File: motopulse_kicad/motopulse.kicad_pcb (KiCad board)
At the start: 2 copper layers, 100 x 95 mm, 12 parts, among them J1 ESP32-S3_Left_Header, J2 ESP32-S3_Right_Header, J3 INMP441_Breakout, J4 OLED_0.96_I2C

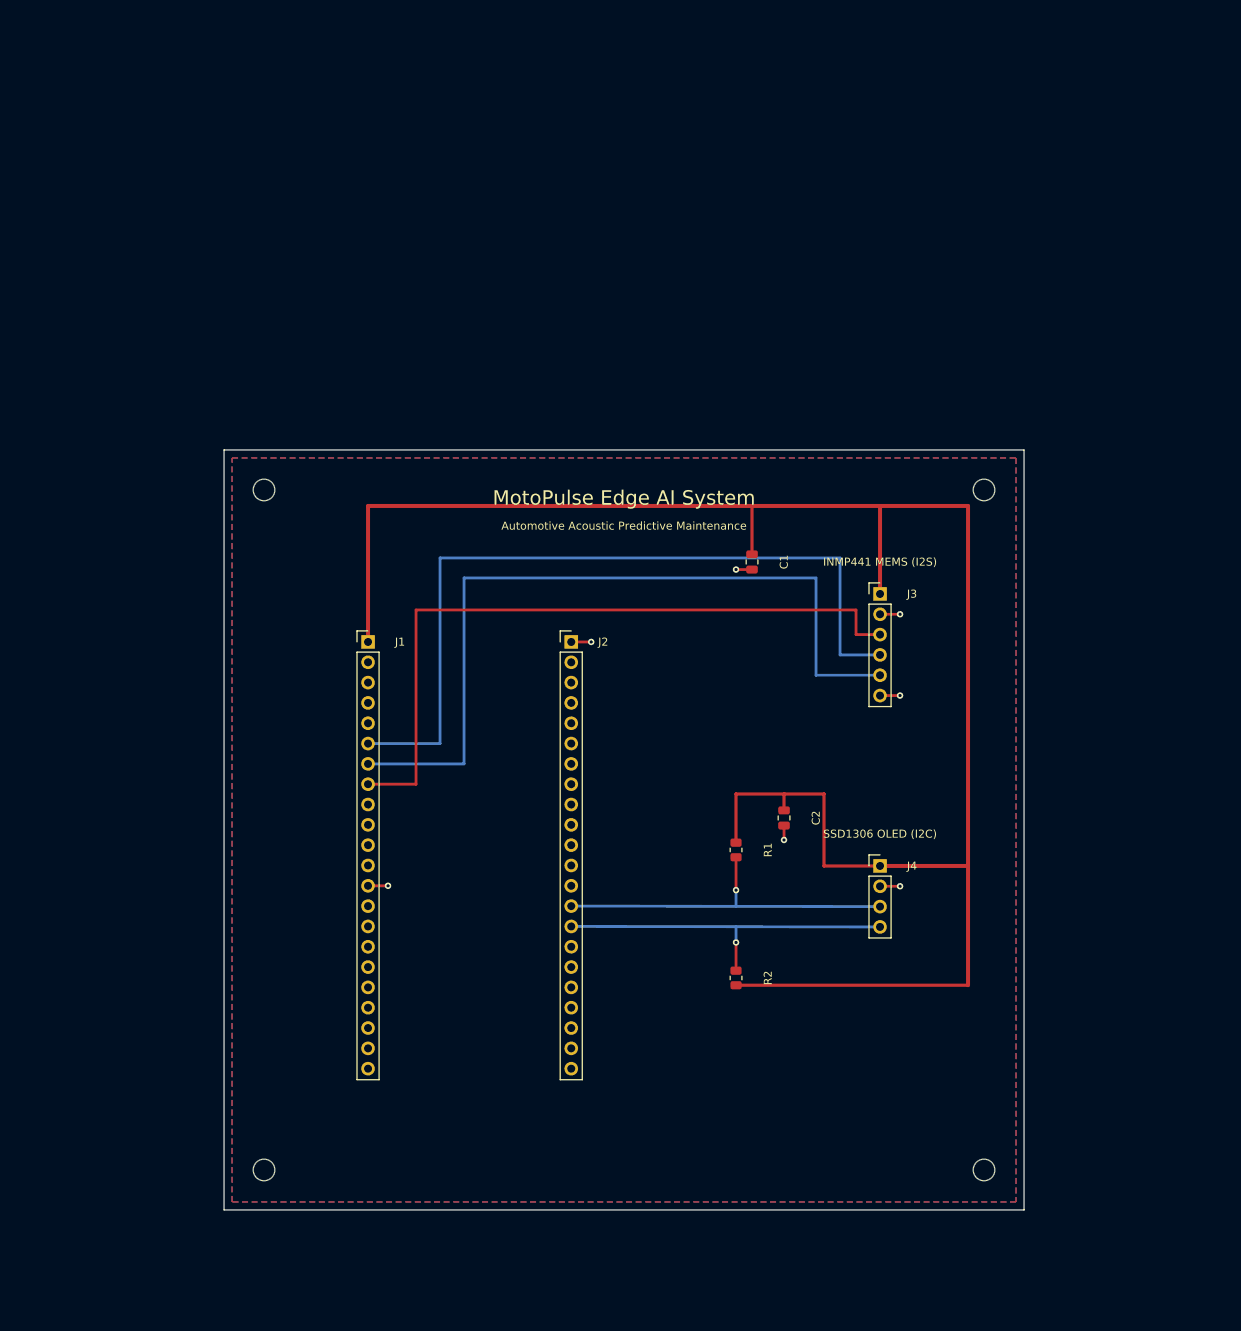
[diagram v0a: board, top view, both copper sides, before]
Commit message: feat(hardware): unified ESP32-S3 carrier with 40mm dual mic, OLED, piezo and zero-capacitor layout
- ESP32-S3-DevKitC-1 (2x22 headers) unified motherboard
- Dual INMP441 MEMS microphones with exactly 40.0 mm baseline spacing
- 0.96 inch SSD1306 OLED display header
- Piezoelectric vibration sensor connector and 1M damping resistor
- Zero capacitors, pure direct-connect architecture
- KiCad ERC 0 errors, PCB DRC 0 violations, 0 unconnected items

Co-authored-by: ishannvn <ishannvn@users.noreply.github.com>
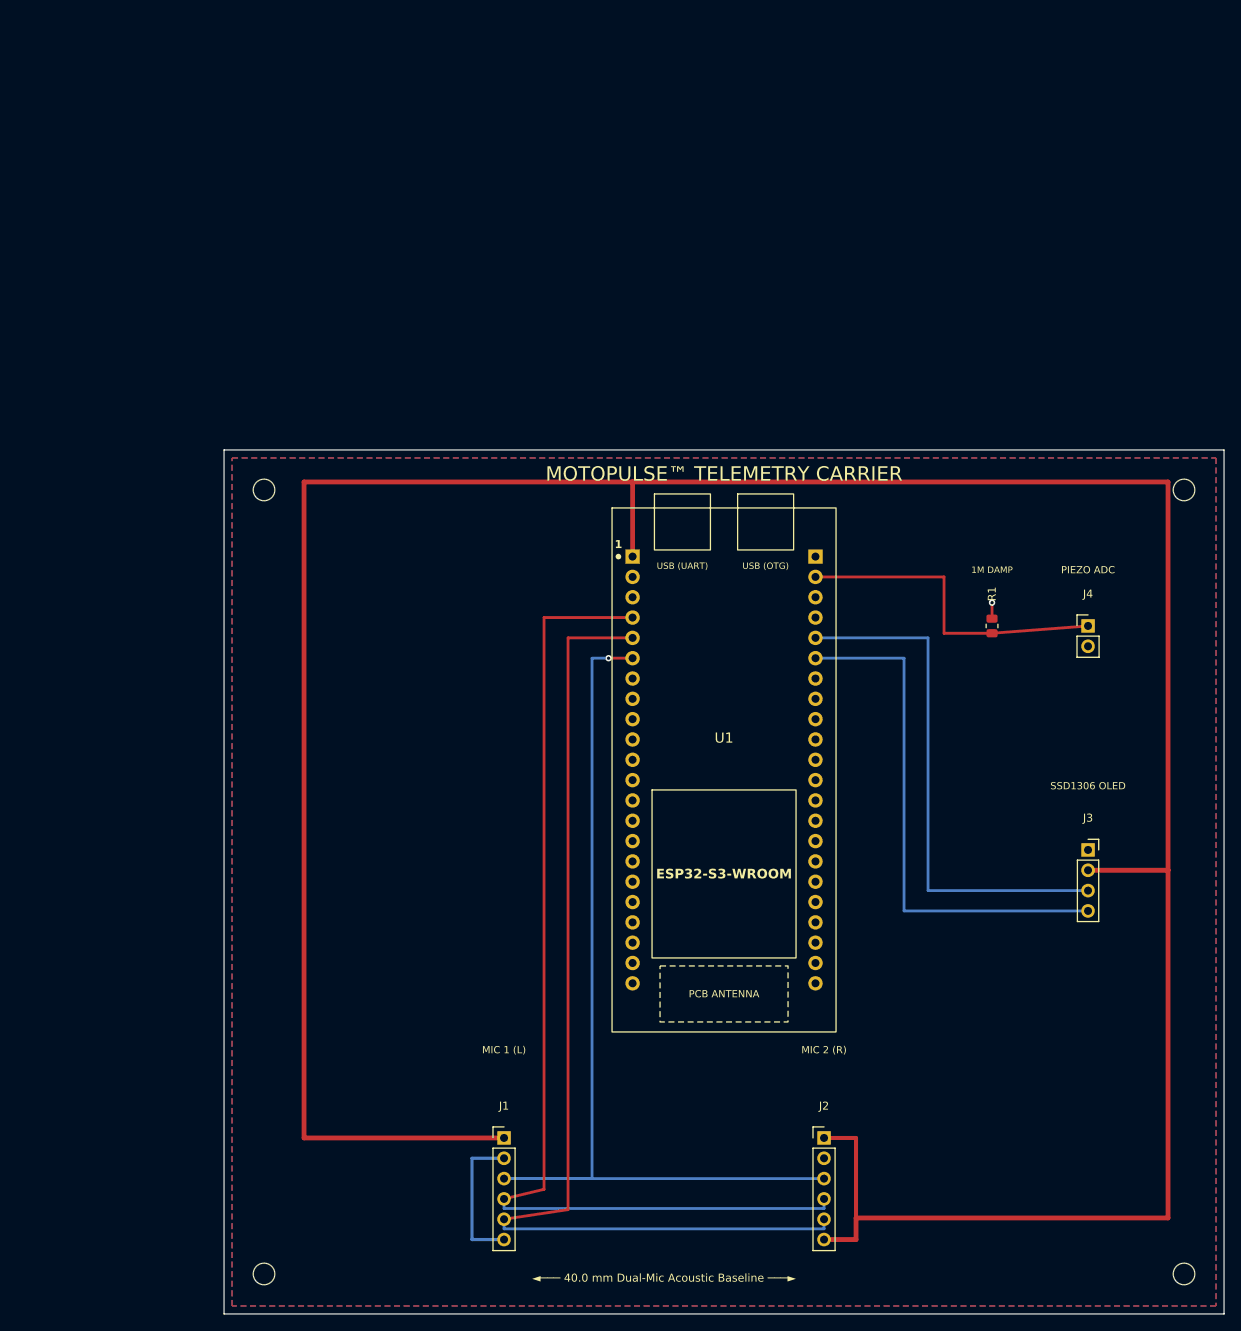
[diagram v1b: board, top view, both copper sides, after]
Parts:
- removed C1, C2: 100nF, C_0805_2012Metric
- removed R2: 4.7k, R_0805_2012Metric
- added U1: ESP32-S3-DevKitC-1, ESP32-S3-DevKitC-1, F.Cu at (162.5, 140.0)
- J1: value ESP32-S3_Left_Header -> INMP441_Left; footprint PinHeader_1x22_P2.54mm_Vertical -> PinHeader_1x06_P2.54mm_Vertical
- J2: value ESP32-S3_Right_Header -> INMP441_Right; footprint PinHeader_1x22_P2.54mm_Vertical -> PinHeader_1x06_P2.54mm_Vertical
- J3: value INMP441_Breakout -> SSD1306_OLED; footprint PinHeader_1x06_P2.54mm_Vertical -> PinSocket_1x04_P2.54mm_Vertical
- J4: value OLED_0.96_I2C -> Piezo_Sensor; footprint PinHeader_1x04_P2.54mm_Vertical -> PinHeader_1x02_P2.54mm_Vertical
- R1: value 4.7k -> 1.0M
- moved J2 69.6 mm to (175.0, 186.0)
- moved J1 64.3 mm to (135.0, 186.0)
- moved R1 42.5 mm to (196.0, 122.0), turned to 90 degrees
- moved J3 41.2 mm to (208.0, 150.0)
- moved J4 39.7 mm to (208.0, 122.0)
- moved H4 28.2 mm to (220.0, 203.0)
- moved H2 25.0 mm to (220.0, 105.0)
- moved H3 13.0 mm to (105.0, 203.0)
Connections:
- J1 pad 2: unconnected-(J1-Pin_2-Pad2) -> GND
- J1 pad 3: unconnected-(J1-Pin_3-Pad3) -> /I2S_SD
- J1 pad 4: unconnected-(J1-Pin_4-Pad4) -> /I2S_SCK
- J1 pad 5: unconnected-(J1-Pin_5-Pad5) -> /I2S_WS
- J1 pad 6: /I2S_SCK -> GND
- J2 pad 1: GND -> +3.3V
- J2 pad 2: unconnected-(J2-Pin_2-Pad2) -> GND
- J2 pad 3: unconnected-(J2-Pin_3-Pad3) -> /I2S_SD
- J2 pad 4: unconnected-(J2-Pin_4-Pad4) -> /I2S_SCK
- J2 pad 5: unconnected-(J2-Pin_5-Pad5) -> /I2S_WS
- J2 pad 6: unconnected-(J2-Pin_6-Pad6) -> +3.3V
- J3 pad 1: +3.3V -> GND
- J3 pad 2: GND -> +3.3V
- J3 pad 3: /I2S_SD -> /I2C_SCL
- J3 pad 4: /I2S_SCK -> /I2C_SDA
- J4 pad 1: +3.3V -> /PIEZO_IN
- R1 pad 1: +3.3V -> /PIEZO_IN
- R1 pad 2: /I2C_SCL -> GND
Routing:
- net +3.3V: track 244.1 -> 392.7 mm
- net /PIEZO_IN: track 0.00 -> 41.1 mm
- net /I2S_SD: track 88.9 -> 121.1 mm, vias 0 -> 1
- net /I2S_SCK: track 99.3 -> 130.1 mm
- net /I2S_WS: track 99.4 -> 130.0 mm
- net /I2C_SDA: track 44.1 -> 65.7 mm, vias 1 -> 0
- net /I2C_SCL: track 44.7 -> 65.7 mm, vias 1 -> 0
- net GND: track 16.3 -> 20.2 mm, vias 7 -> 1
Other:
- board size 100 x 95 mm -> 125 x 108 mm
- board text added: "1M DAMP"
- board text added: "MIC 1 (L)"
- board text added: "MIC 2 (R)"
- board text added: "MOTOPULSE™ TELEMETRY CARRIER"
- board text added: "PIEZO ADC"
- board text added: "SSD1306 OLED"
- board text added: "◄─── 40.0 mm Dual-Mic Acoustic Baseline ───►"
- board text removed: "Automotive Acoustic Predictive Maintenance"
- board text removed: "INMP441 MEMS (I2S)"
- board text removed: "MotoPulse Edge AI System"
- board text removed: "SSD1306 OLED (I2C)"

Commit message: fix(hardware): update KiCad schematic and PCB to match ESP32-S3-DevKitC-1-N16R8 pinout
- Updated 44-pin schematic symbol to official ESP32-S3-DevKitC-1-N16R8 pin layout
- Corrected J1 header pins (1-22) with 3V3, RST, GPIO4-6, GPIO7-21, GND
- Corrected J3 header pins (23-44) with 3V3, 5V, GND, GPIO1 (Piezo), GPIO41/40 (I2C OLED), Octal PSRAM reservation (GPIO35-37), GND
- Updated silkscreen labels and board footprint to ESP32-S3-WROOM-1 N16R8
- Verified 0 ERC violations and 0 PCB DRC violations (0 unconnected items)

Co-authored-by: ishannvn <ishannvn@users.noreply.github.com>
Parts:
- U1: value ESP32-S3-DevKitC-1 -> ESP32-S3-DevKitC-1-N16R8
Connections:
- U1 pad 22: unconnected-(U1-GPIO14-Pad22) -> GND
- U1 pad 23: GND -> unconnected-(U1-3V3-Pad23)
- U1 pad 24: /PIEZO_IN -> unconnected-(U1-5V-Pad24)
- U1 pad 25: unconnected-(U1-GPIO2-Pad25) -> GND
- U1 pad 26: unconnected-(U1-GPIO42-Pad26) -> /PIEZO_IN
- U1 pad 27: /I2C_SCL -> unconnected-(U1-GPIO2-Pad27)
- U1 pad 28: /I2C_SDA -> unconnected-(U1-GPIO42-Pad28)
- U1 pad 29: unconnected-(U1-GPIO39-Pad29) -> /I2C_SCL
- U1 pad 30: unconnected-(U1-GPIO38-Pad30) -> /I2C_SDA
- U1 pad 41: GND -> unconnected-(U1-RX_GPIO44-Pad41)
- U1 pad 42: GND -> unconnected-(U1-D-_GPIO19-Pad42)
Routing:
- net /I2C_SDA: track 65.7 -> 60.6 mm
- net /PIEZO_IN: track 41.1 -> 36.1 mm
- net /I2C_SCL: track 65.7 -> 60.6 mm

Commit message: fix(hardware): route OLED I2C SCL to GPIO 8 and SDA to GPIO 9
- Reconnected 0.96 inch SSD1306 OLED I2C lines:
  - SCL -> GPIO 8 (Pin 12 on ESP32-S3-DevKitC-1-N16R8)
  - SDA -> GPIO 9 (Pin 15 on ESP32-S3-DevKitC-1-N16R8)
- Updated PCB router with layer-separated orthogonal paths around U1
- Verified 0 ERC violations and 0 PCB DRC violations with 0 unconnected items

Co-authored-by: ishannvn <ishannvn@users.noreply.github.com>
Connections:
- U1 pad 12: unconnected-(U1-GPIO8-Pad12) -> /I2C_SCL
- U1 pad 15: unconnected-(U1-GPIO9-Pad15) -> /I2C_SDA
- U1 pad 29: /I2C_SCL -> unconnected-(U1-GPIO41-Pad29)
- U1 pad 30: /I2C_SDA -> unconnected-(U1-GPIO40-Pad30)
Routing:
- net /I2C_SCL: track 60.6 -> 105.7 mm
- net /I2C_SDA: track 60.6 -> 104.6 mm

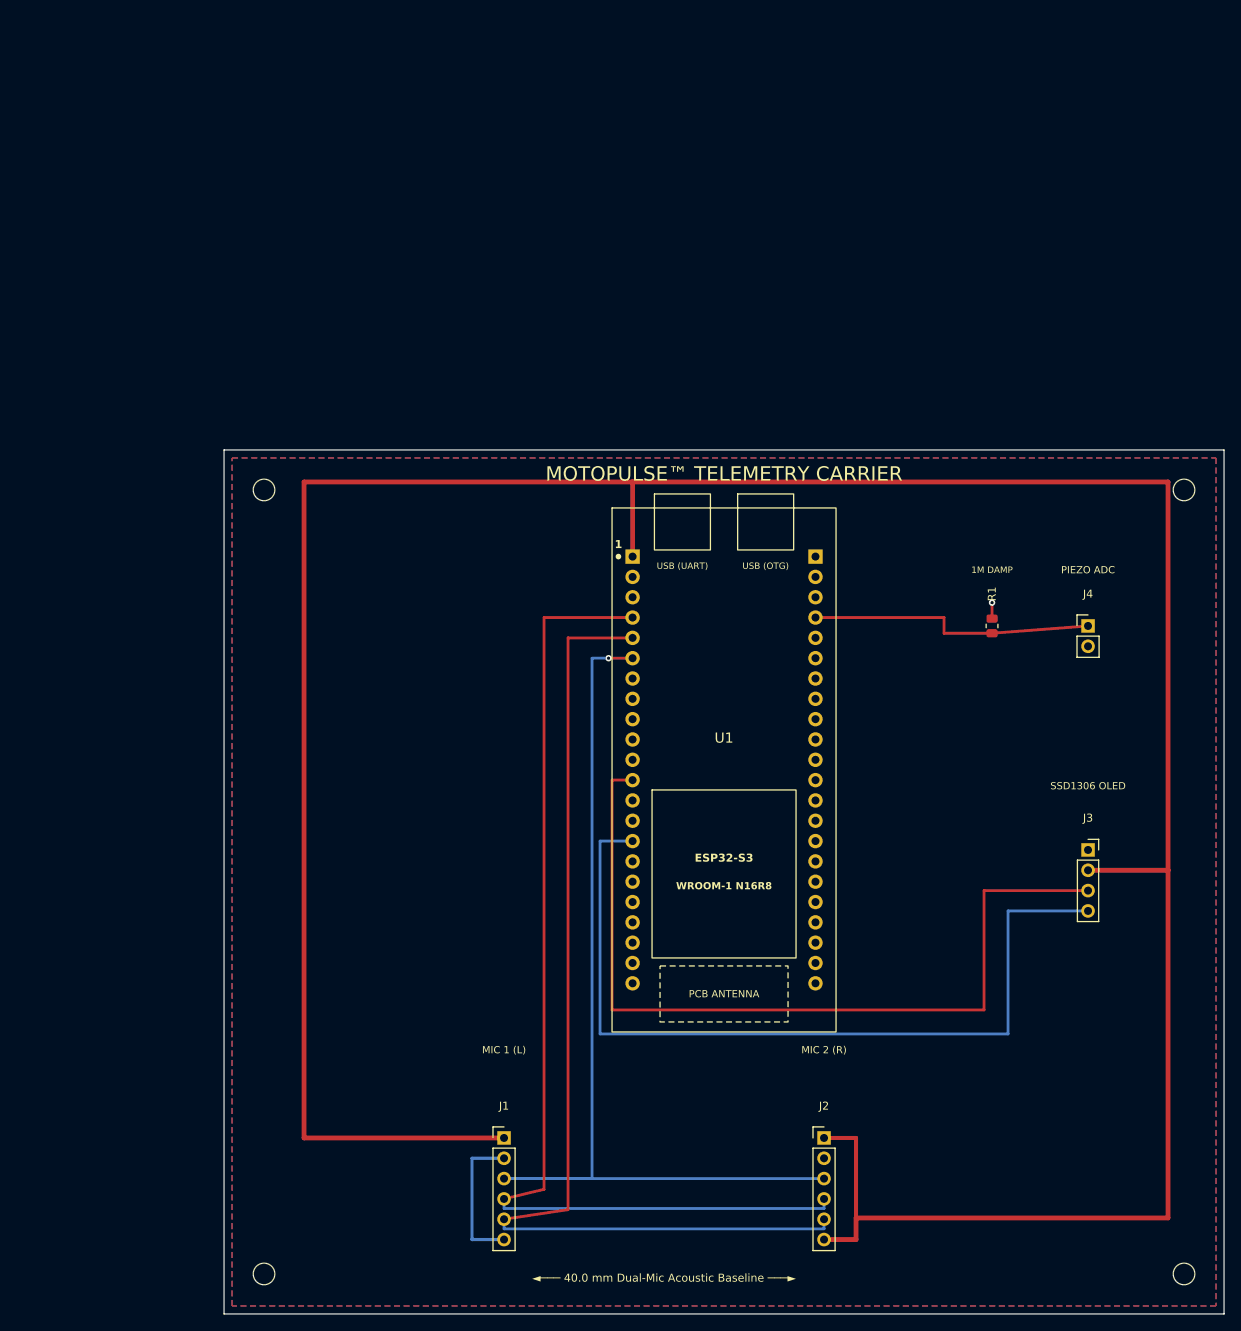
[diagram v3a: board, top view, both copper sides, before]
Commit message: feat: implement autonomous continual self-learning engine and live telemetry dashboard
- Deploy embedded C++ Online Continual Learning Engine (ESP32OnlineVehicleLearner) with Welford streaming EMA adaptation
- Implement engine running verification gating via Piezo (GPIO 1) + I2S acoustic energy
- Add Anomaly Drift Guard freezing baseline updates during acoustic/vibration defects (>3.2 sigma)
- Add NVS Flash persistence saving vehicle profile across ignition cycles
- Add Arduino firmware sketch (firmware/motopulse_online_learner.ino) with FreeRTOS task on Core 1
- Integrate real-time continual learner telemetry into dashboard/server.py and web UI
- Add live self-learning status, operational regimes, Z-meter, and interactive demo controls in Cockpit UI
- Preserve user edits in KiCad carrier board schematic and PCB

Co-authored-by: ishannvn <ishannvn@users.noreply.github.com>
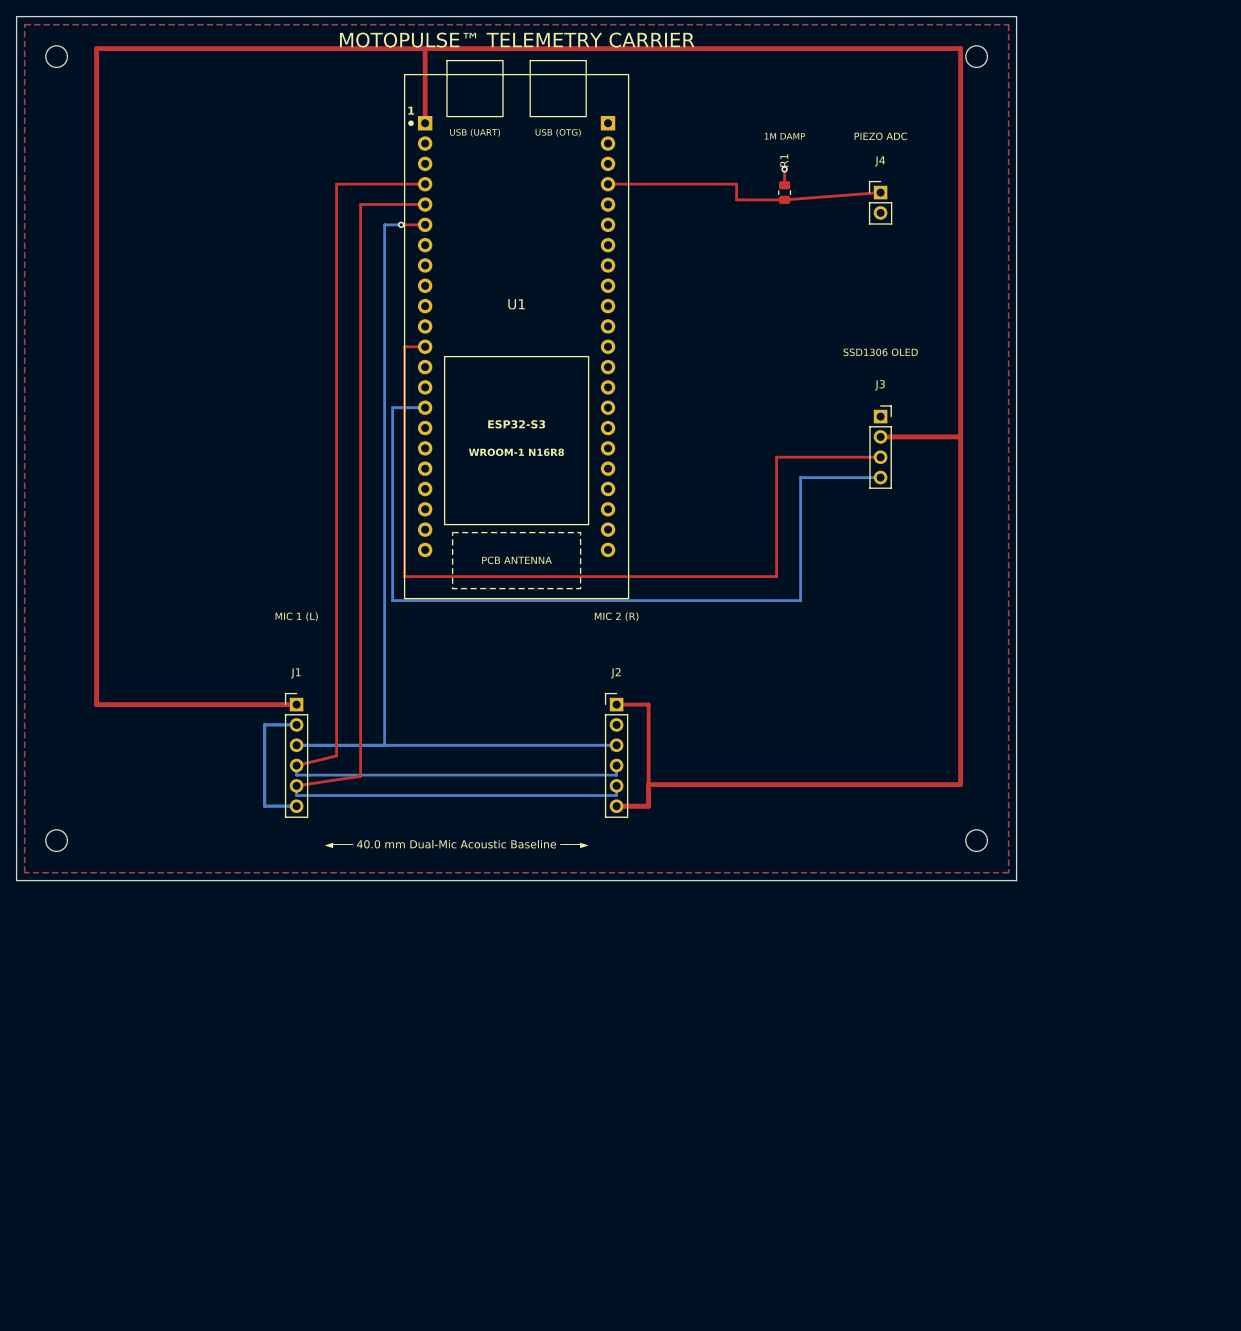
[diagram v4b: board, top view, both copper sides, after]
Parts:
- moved H1 60.1 mm to (79.1, 50.8)
- moved H2 60.1 mm to (194.1, 50.8)
- moved J3 60.1 mm to (182.1, 95.8)
- moved J4 60.1 mm to (182.1, 67.8)
- moved R1 60.1 mm to (170.1, 67.8)
- moved U1 60.1 mm to (136.6, 85.8)
- moved H3 60.1 mm to (79.1, 148.8)
- moved H4 60.1 mm to (194.1, 148.8)
- moved J1 60.1 mm to (109.1, 131.8)
- moved J2 60.1 mm to (149.1, 131.8)
